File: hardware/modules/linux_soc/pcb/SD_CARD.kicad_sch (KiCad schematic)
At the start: 1 part

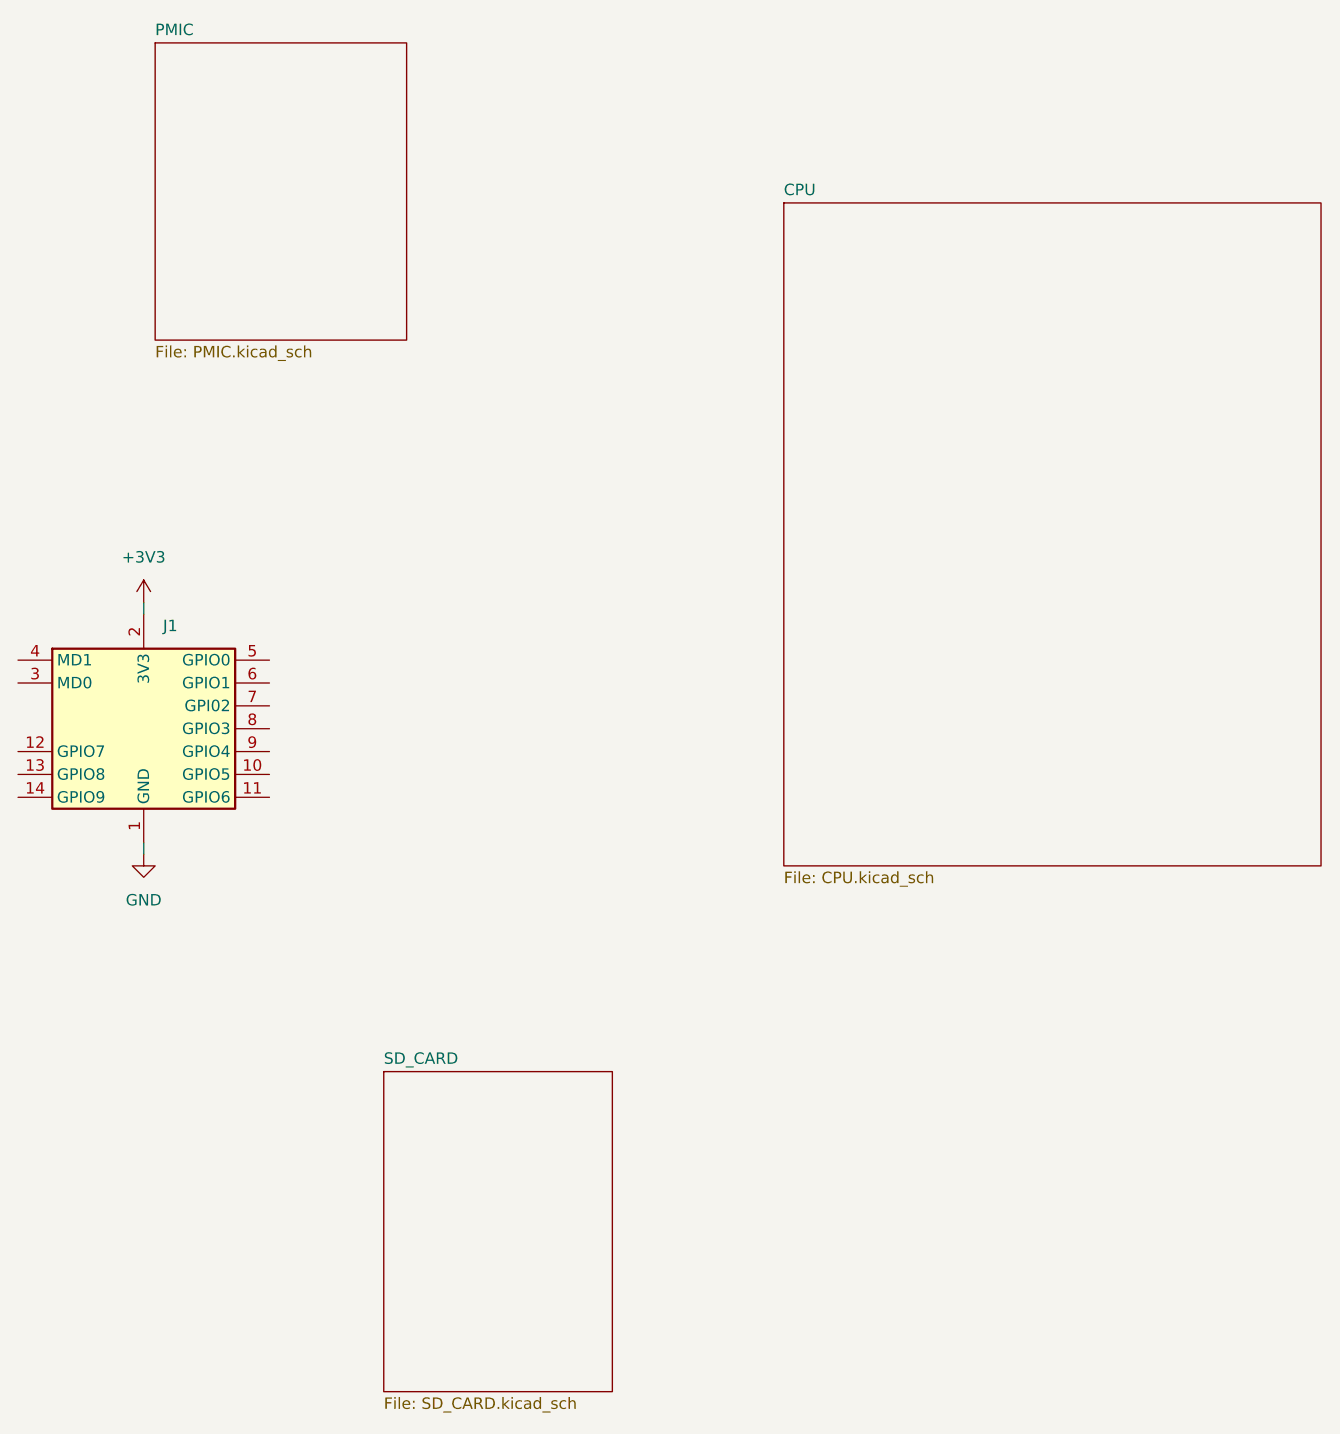
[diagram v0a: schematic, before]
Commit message: Added Crystal and SD card to linux soc card
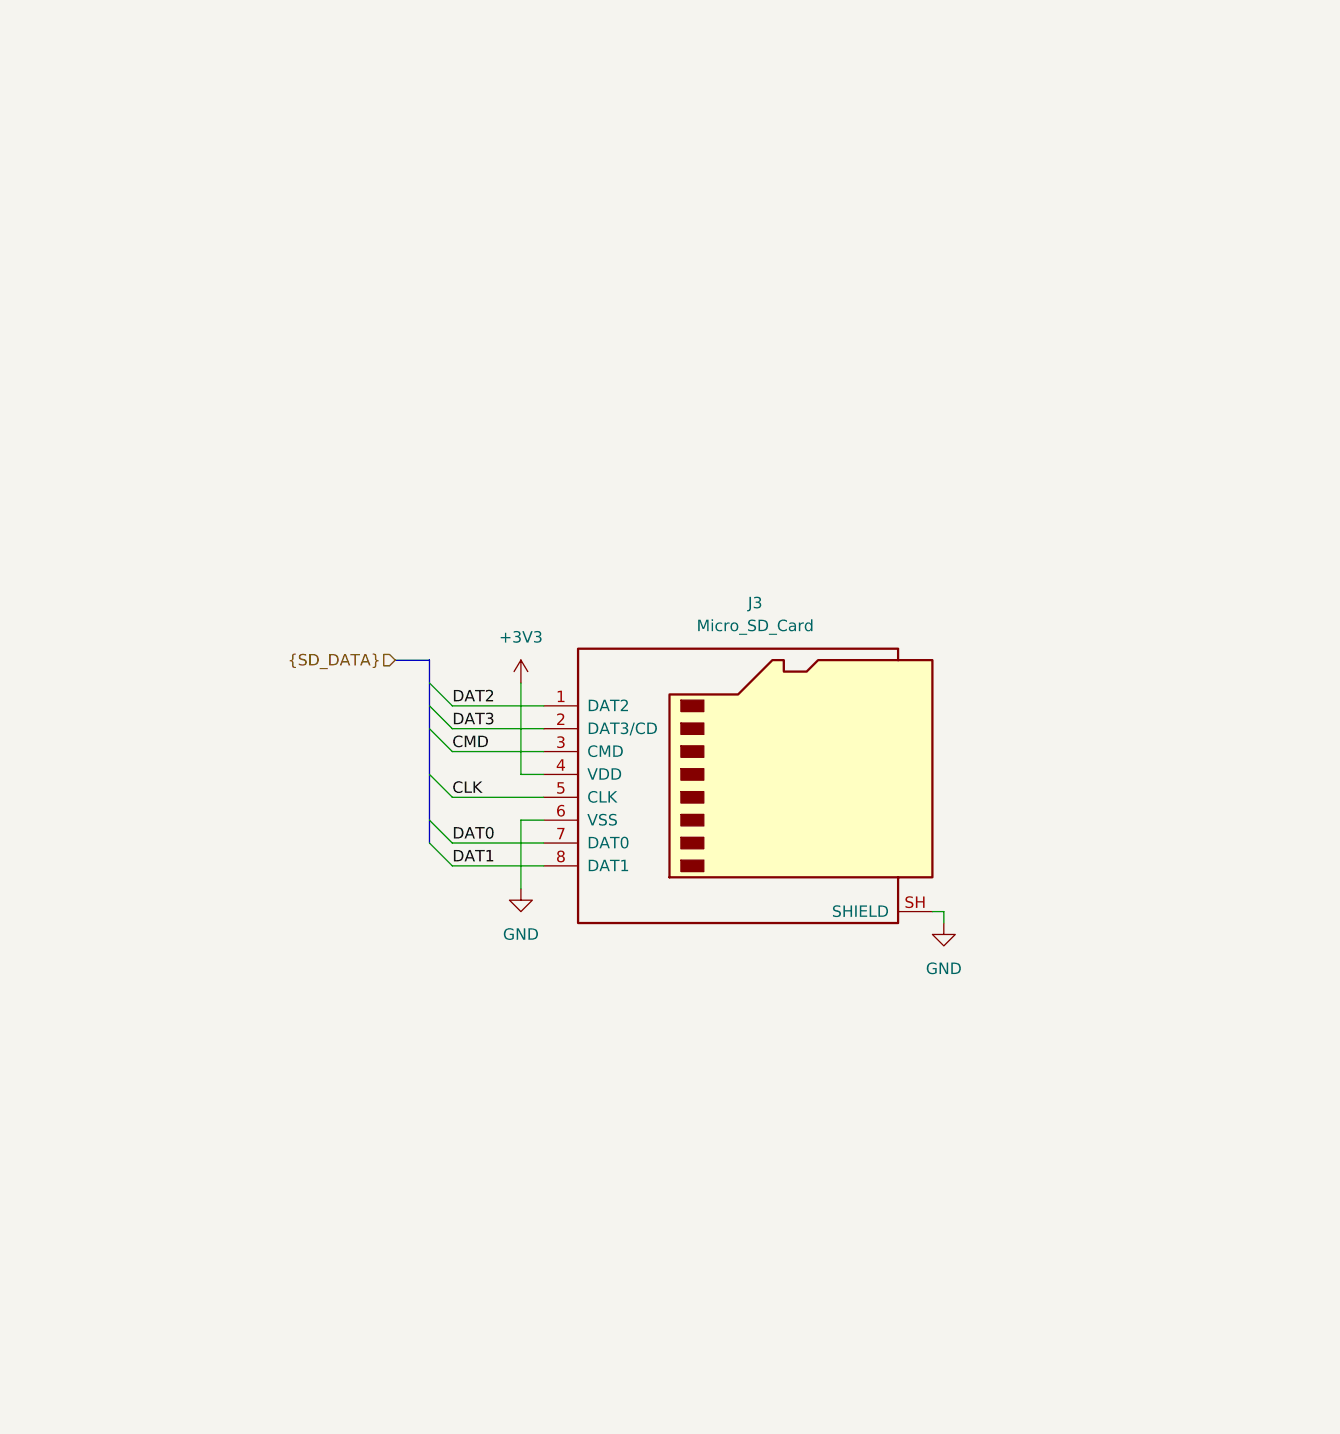
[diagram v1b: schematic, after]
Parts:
- removed J1: (no value), Connector_PinHeader_2.54mm:PinHeader_2x07_P2.54mm_Horizontal, symbol Hackxpansion:Module_Male
- added J3: Micro_SD_Card, symbol Connector:Micro_SD_Card
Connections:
- net +3V3: now also J3.4 (VDD)
- net GND: now also J3.6 (VSS), J3.SH (SHIELD)
- new net CLK: J3.5 (CLK)
- new net CMD: J3.3 (CMD)
- new net DAT0: J3.7 (DAT0)
- new net DAT1: J3.8 (DAT1)
- new net DAT2: J3.1 (DAT2)
- new net DAT3: J3.2 (DAT3/CD)
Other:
- removed sheet CPU
- removed sheet PMIC
- removed sheet SD_CARD

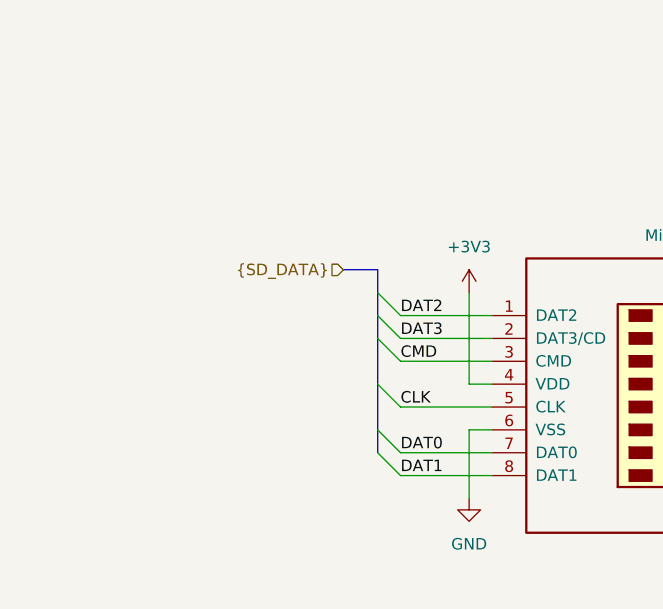
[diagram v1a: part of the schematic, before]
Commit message: Started on PCB layout finished schematic
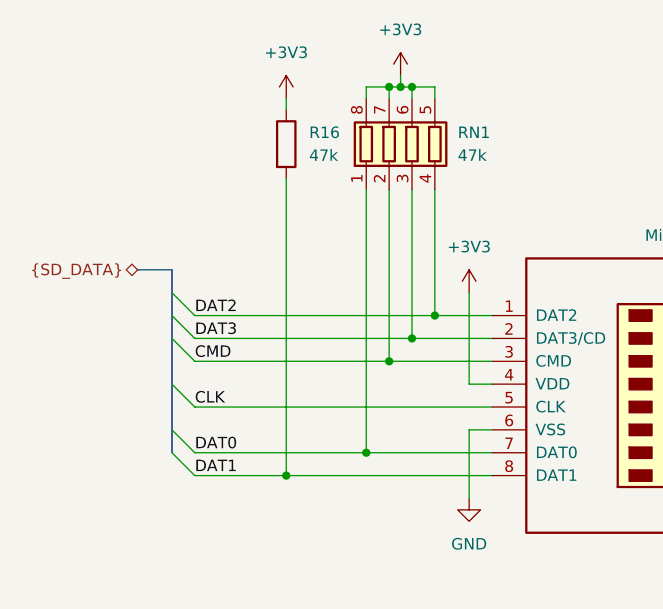
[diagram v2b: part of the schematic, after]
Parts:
- added R16: 47k, Resistor_SMD:R_0402_1005Metric, symbol Device:R
- added RN1: 47k, Resistor_SMD:R_Array_Convex_4x0402, symbol Device:R_Pack04
- J3: footprint (none) -> Connector_Card:microSD_HC_Hirose_DM3AT-SF-PEJM5; LCSC# (none) -> C114218
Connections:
- net +3V3: now also R16.1, RN1.5 (R4.2), RN1.6 (R3.2), RN1.7 (R2.2), RN1.8 (R1.2)
- net CMD: now also RN1.2 (R2.1)
- net DAT0: now also RN1.1 (R1.1)
- net DAT1: now also R16.2
- net DAT2: now also RN1.4 (R4.1)
- net DAT3: now also RN1.3 (R3.1)
